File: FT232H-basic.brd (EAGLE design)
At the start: 45.7 x 20.3 mm, 29 parts, among them IC1 FT232H

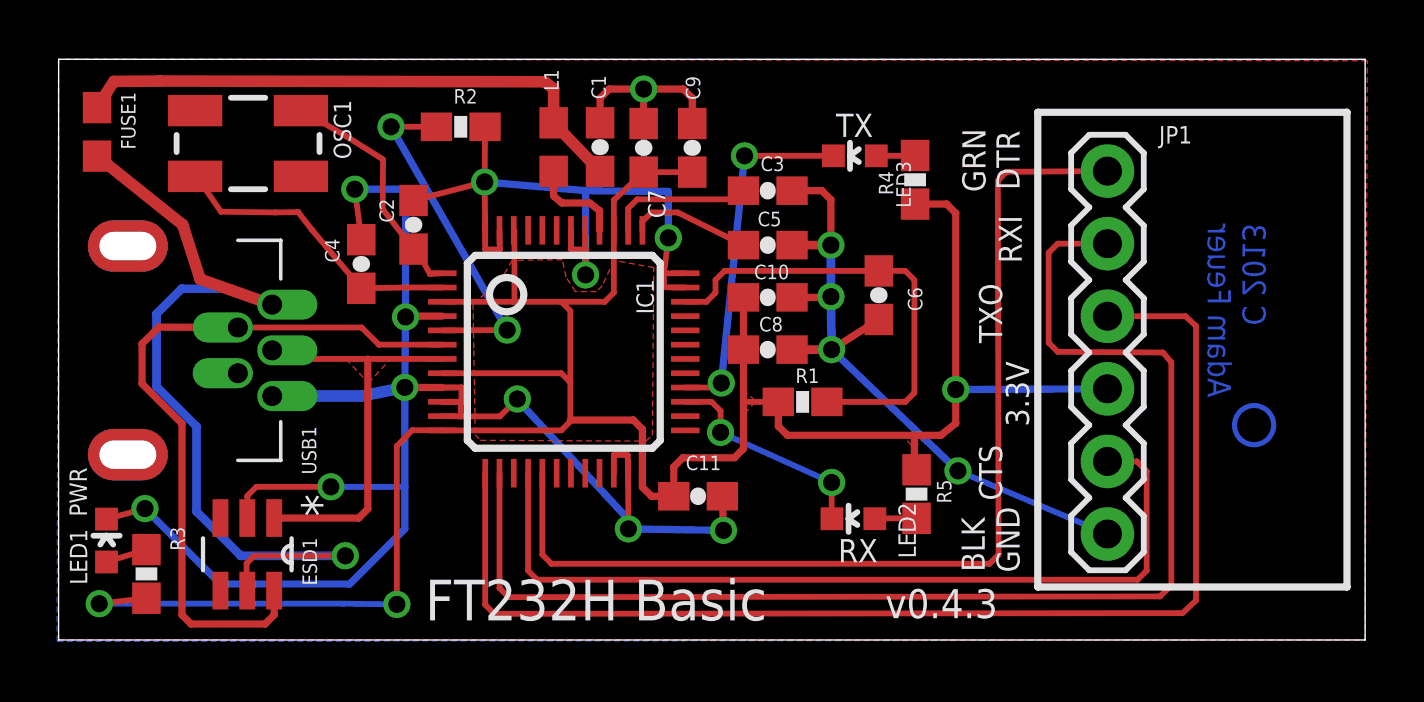
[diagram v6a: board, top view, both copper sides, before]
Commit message: corrected RX and TX LED circuit
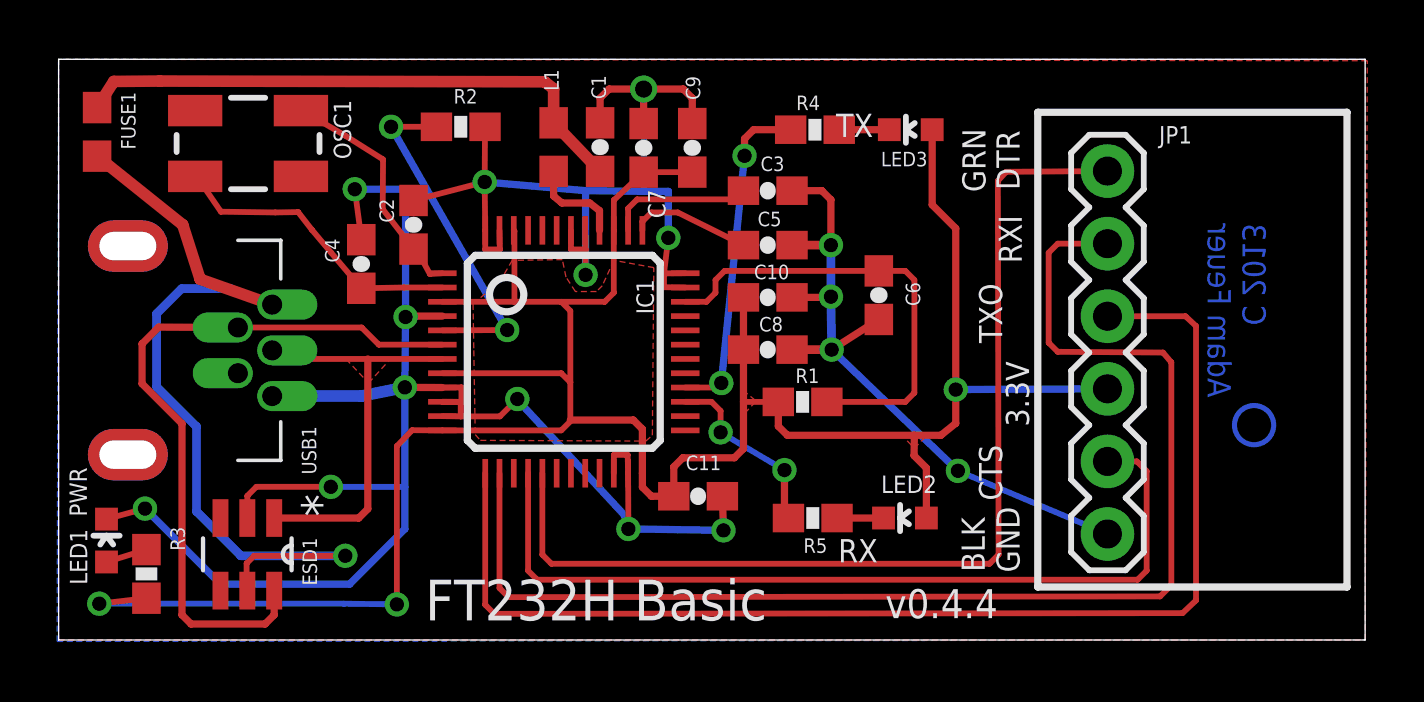
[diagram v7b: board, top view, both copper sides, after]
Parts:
- moved R4 3.92 mm to (32.8, 21.7), turned to 180 degrees
- moved R5 3.73 mm to (32.7, 8.08), turned to 180 degrees
- moved LED3 2.16 mm to (36.2, 21.7)
- moved LED2 1.80 mm to (36.0, 8.08)
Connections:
- net N$10: now also LED2.C, R5.1; no longer LED2.A, R5.2
- net N$8: now also LED3.C, R4.1; no longer LED3.A, R4.2
- net POWER: now also LED2.A, LED3.A; no longer R4.1, R5.1
- net RXLED: now also R5.2; no longer LED2.C
- net TXLED: now also R4.2; no longer LED3.C
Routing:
- net POWER: track 86.9 -> 90.5 mm
- net RXLED: track 7.66 -> 6.45 mm
- net TXLED: track 12.4 -> 11.7 mm
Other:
- board text added: "v0.4.4"
- board text removed: "v0.4.3"
